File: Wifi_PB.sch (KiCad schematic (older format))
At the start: 0 parts

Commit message: version preliminar de la etapa de alimentacion
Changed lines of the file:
@@
 LIBS:Sensores
 LIBS:Reles
+LIBS:Reguladores
+LIBS:Transistores
 LIBS:Wifi_PB-cache
 EELAYER 26 0
@@
 $Descr A4 11693 8268
 encoding utf-8
-Sheet 1 11
+Sheet 1 15
 Title ""
 Date "2017-01-15"
@@
 $EndDescr
 $Sheet
-S 4150 3100 1400 1000
+S 4100 3100 1250 850
 U 583E04A5
 F0 "Alimentacion" 60
@@
 $EndSheet
 $Sheet
-S 4150 1600 1400 1000
+S 4100 1600 1250 850
 U 583CB21E
 F0 "Control" 60
@@
 $EndSheet
 $Sheet
-S 7250 1600 1400 1000
+S 7250 1600 1250 850
 U 587ABB4C
 F0 "PWM" 60
@@
 $EndSheet
 $Sheet
-S 5700 1600 1400 1000
+S 5700 1600 1250 850
 U 583F2D05
 F0 "Matriz_Led" 60
@@
 F1 "Conectores_E_S.sch" 60
 $EndSheet
+$Sheet
+S 8800 3100 1400 1000
+U 588EAC0E
+F0 "Ultrasonidos" 60
+F1 "Ultrasonidos.sch" 60
+$EndSheet
+$Sheet
+S 8800 4700 1400 1000
+U 588EAF83
+F0 "Infrarrojos" 60
+F1 "Infrarrojos.sch" 60
+$EndSheet
+$Sheet
+S 2150 1650 1250 850
+U 588EB646
+F0 "Potenciometro" 60
+F1 "Potenciometro.sch" 60
+$EndSheet
+$Sheet
+S 2150 3100 1250 850
+U 588EBE10
+F0 "Buzzer" 60
+F1 "Buzzer.sch" 60
+$EndSheet
 $EndSCHEMATC

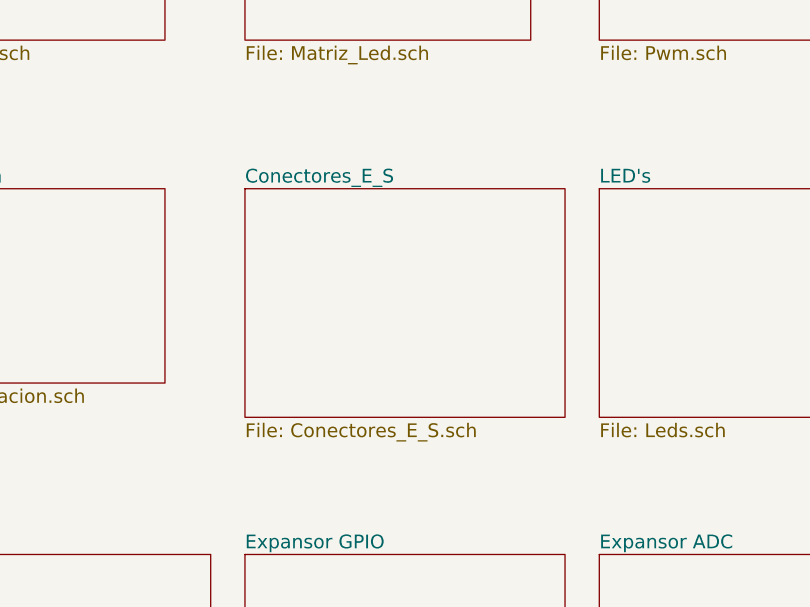
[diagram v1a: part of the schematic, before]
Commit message: asignacion inicial de huellas
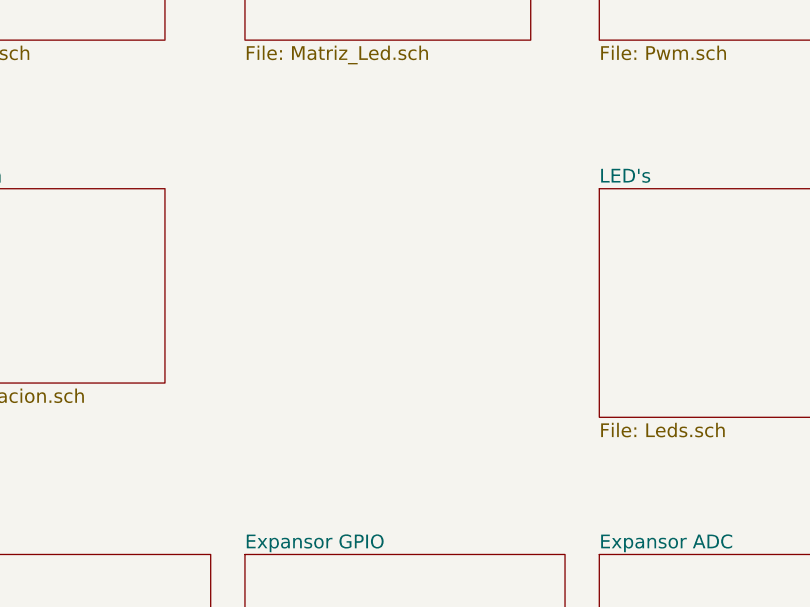
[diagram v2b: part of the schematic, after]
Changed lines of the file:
@@
-$EndSheet
-$Sheet
-S 5700 3100 1400 1000
-U 583F7030
-F0 "Conectores_E_S" 60
-F1 "Conectores_E_S.sch" 60
 $EndSheet
 $Sheet

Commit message: añadida LDR. Finalizado trazado provisional
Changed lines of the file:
@@
 $Descr A4 11693 8268
 encoding utf-8
-Sheet 1 14
+Sheet 1 15
 Title ""
 Date "2017-01-15"
@@
 $EndSheet
 $Sheet
-S 8800 1600 1400 1000
+S 8800 1600 1250 850
 U 587C6740
 F0 "Acelerometro" 60
@@
 $EndSheet
 $Sheet
-S 5700 4700 1400 1000
+S 5700 4700 1250 850
 U 587AB37A
 F0 "Expansor GPIO" 60
@@
 $EndSheet
 $Sheet
-S 7250 4700 1400 1000
+S 7250 4700 1250 850
 U 587AB37D
 F0 "Expansor ADC" 60
@@
 $EndSheet
 $Sheet
-S 7250 3100 1400 1000
+S 7250 3100 1250 850
 U 587C425D
 F0 "LED's" 60
@@
 $EndSheet
 $Sheet
-S 4150 4700 1400 1000
+S 4150 4700 1250 850
 U 587C427E
 F0 "Pulsadores" 60
@@
 $EndSheet
 $Sheet
-S 8800 3100 1400 1000
+S 8800 3100 1250 850
 U 588EAC0E
 F0 "Ultrasonidos" 60
@@
 $EndSheet
 $Sheet
-S 8800 4700 1400 1000
+S 8800 4700 1250 850
 U 588EAF83
 F0 "Infrarrojos" 60
@@
 F1 "Buzzer.sch" 60
 $EndSheet
+$Sheet
+S 5700 3100 1250 850
+U 589DE393
+F0 "LDR" 60
+F1 "LDR.sch" 60
+$EndSheet
 $EndSCHEMATC
